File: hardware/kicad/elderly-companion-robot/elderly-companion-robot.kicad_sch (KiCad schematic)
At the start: 0 parts

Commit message: Phase 3: Create 6 hierarchical sheets
- Power_Supply (buck converter, LDO, charger)
- MCU_Core (ESP32-S3-WROOM-1, boot/EN, decoupling)
- Motor_Driver (L298N, flyback diodes, motor connectors)
- Sensors (HC-SR04 x4, MPU6050, SSD1306, I2C pull-ups)
- Audio (INMP441 mic, MAX98357A amp, speaker)
- Camera_Dock (ESP32-CAM, servos, IR beacon, dock contact)

Sheet size set to A2 for all components.

Co-Authored-By: Claude Opus 4.7 <noreply@anthropic.com>
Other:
- added sheet Audio (audio.kicad_sch)
- added sheet Camera_Dock (camera_dock.kicad_sch)
- added sheet MCU_Core (mcu_core.kicad_sch)
- added sheet Motor_Driver (motor_driver.kicad_sch)
- added sheet Power_Supply (power_supply.kicad_sch)
- added sheet Sensors (sensors.kicad_sch)

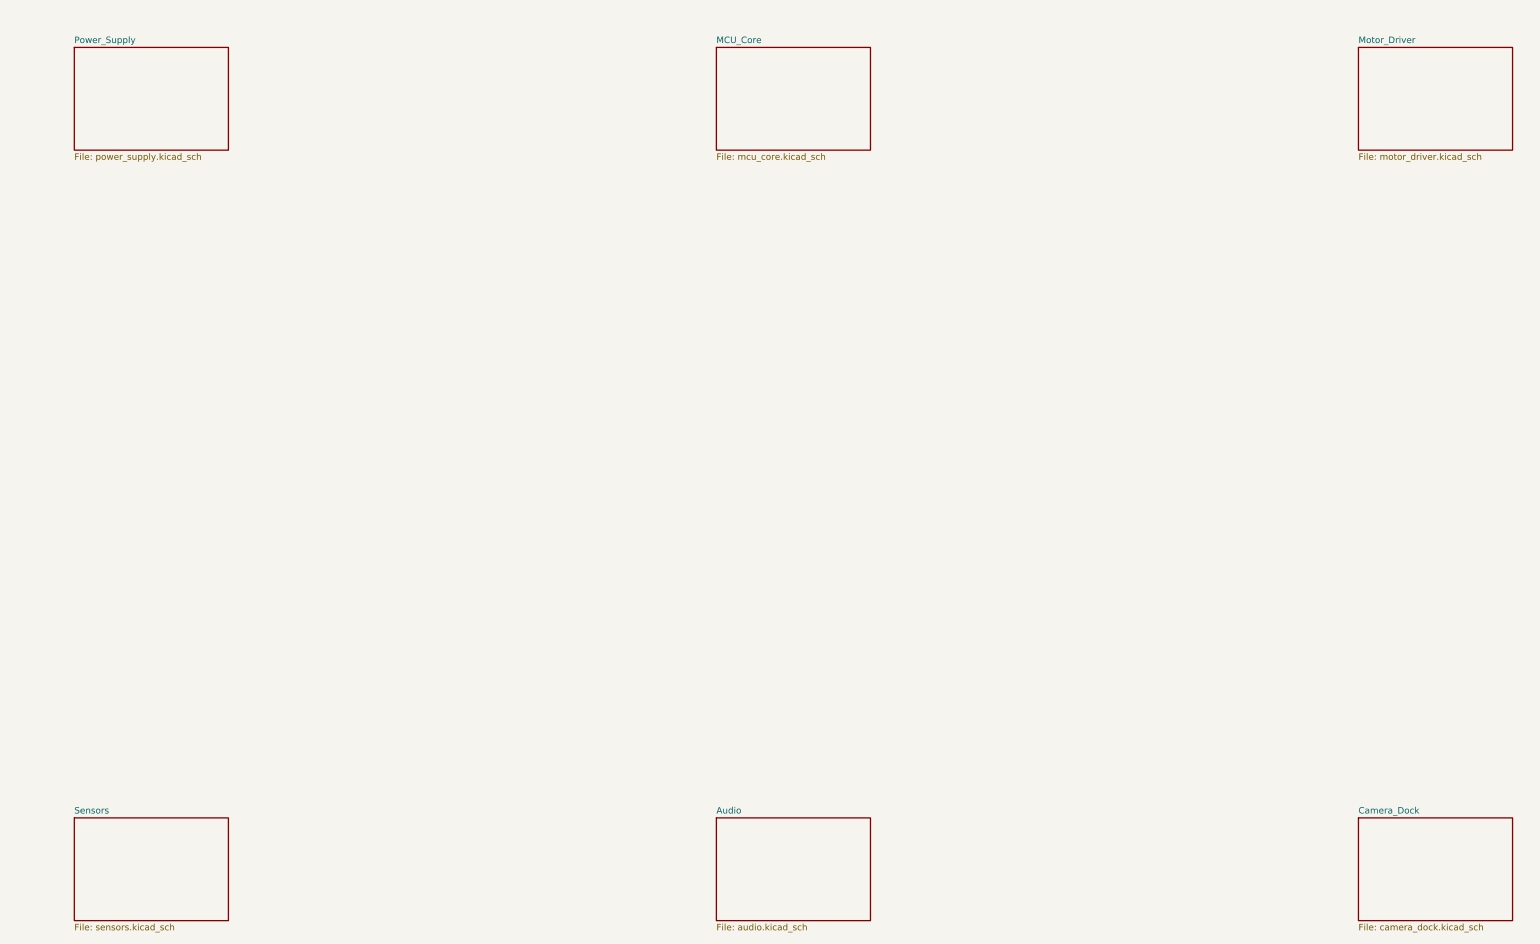
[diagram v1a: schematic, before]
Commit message: Phase 4 WIP: Power supply components placed (symbols only, not yet wired)
- LM2596S-5 buck converter (U3)
- AP2112K-3.3 LDO (U5)
- TP4056-42-ESOP8 charger (U6)
- Battery connector (J_BAT) and dock charge connector (J_DOCK)
- Passive components: C1-C5, L1, D1, R1-R3, LED1-LED2
- Power symbols: +5V, +3V3, GND, VBAT global label
- 46 ERC errors expected (pins not yet wired)

Co-Authored-By: Claude Opus 4.7 <noreply@anthropic.com>
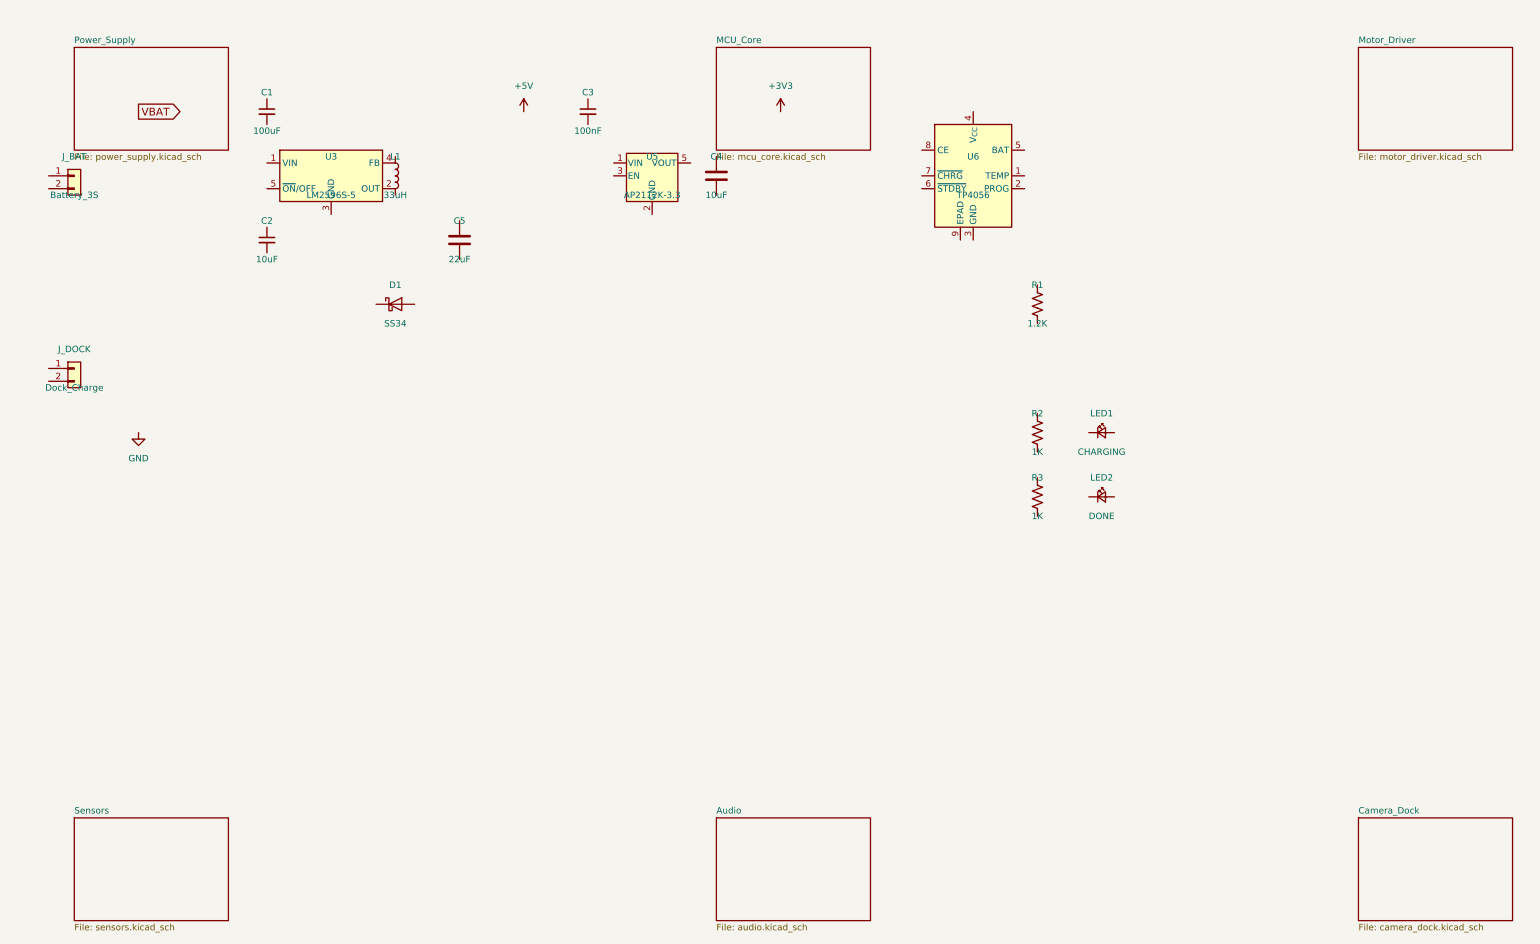
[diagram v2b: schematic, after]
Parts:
- added C1: 100uF, symbol Device:C_Small
- added C2: 10uF, symbol Device:C_Small
- added C3: 100nF, symbol Device:C_Small
- added C4: 10uF, symbol Device:C
- added C5: 22uF, symbol Device:C
- added D1: SS34, symbol Device:D_Schottky
- added J_BAT: Battery_3S, symbol Connector_Generic:Conn_01x02
- added J_DOCK: Dock_Charge, symbol Connector_Generic:Conn_01x02
- added L1: 33uH, symbol Device:L
- added LED1: CHARGING, symbol Device:LED_Small
- added LED2: DONE, symbol Device:LED_Small
- added R1: 1.2K, symbol Device:R_US
- added R2, R3: 1K, symbol Device:R_US
- added U3: LM2596S-5, symbol Regulator_Switching:LM2596S-5
- added U5: AP2112K-3.3, symbol Regulator_Linear:AP2112K-3.3
- added U6: TP4056, symbol Battery_Management:TP4056-42-ESOP8

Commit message: Phase 4 WIP: Power supply components + SIM800L LDO placed, global labels added
- Added AMS1117 adjustable LDO (U7) for SIM800L 4V rail (5V→4V)
- Added C6 100uF (SIM800L LDO input bypass)
- Added C7 10uF (SIM800L LDO output filter)
- Added C8 470uF (SIM800L burst capacitor for 2A peak)
- Added R4 1K + R5 2.2K voltage divider (sets LDO output to 4.0V)
- Added +4V global label and power symbol
- Added VBAT, +5V, +3V3 global labels
- All 27 power supply components now placed on sheet
- Detailed wiring to be completed next

Co-Authored-By: Claude Opus 4.7 <noreply@anthropic.com>
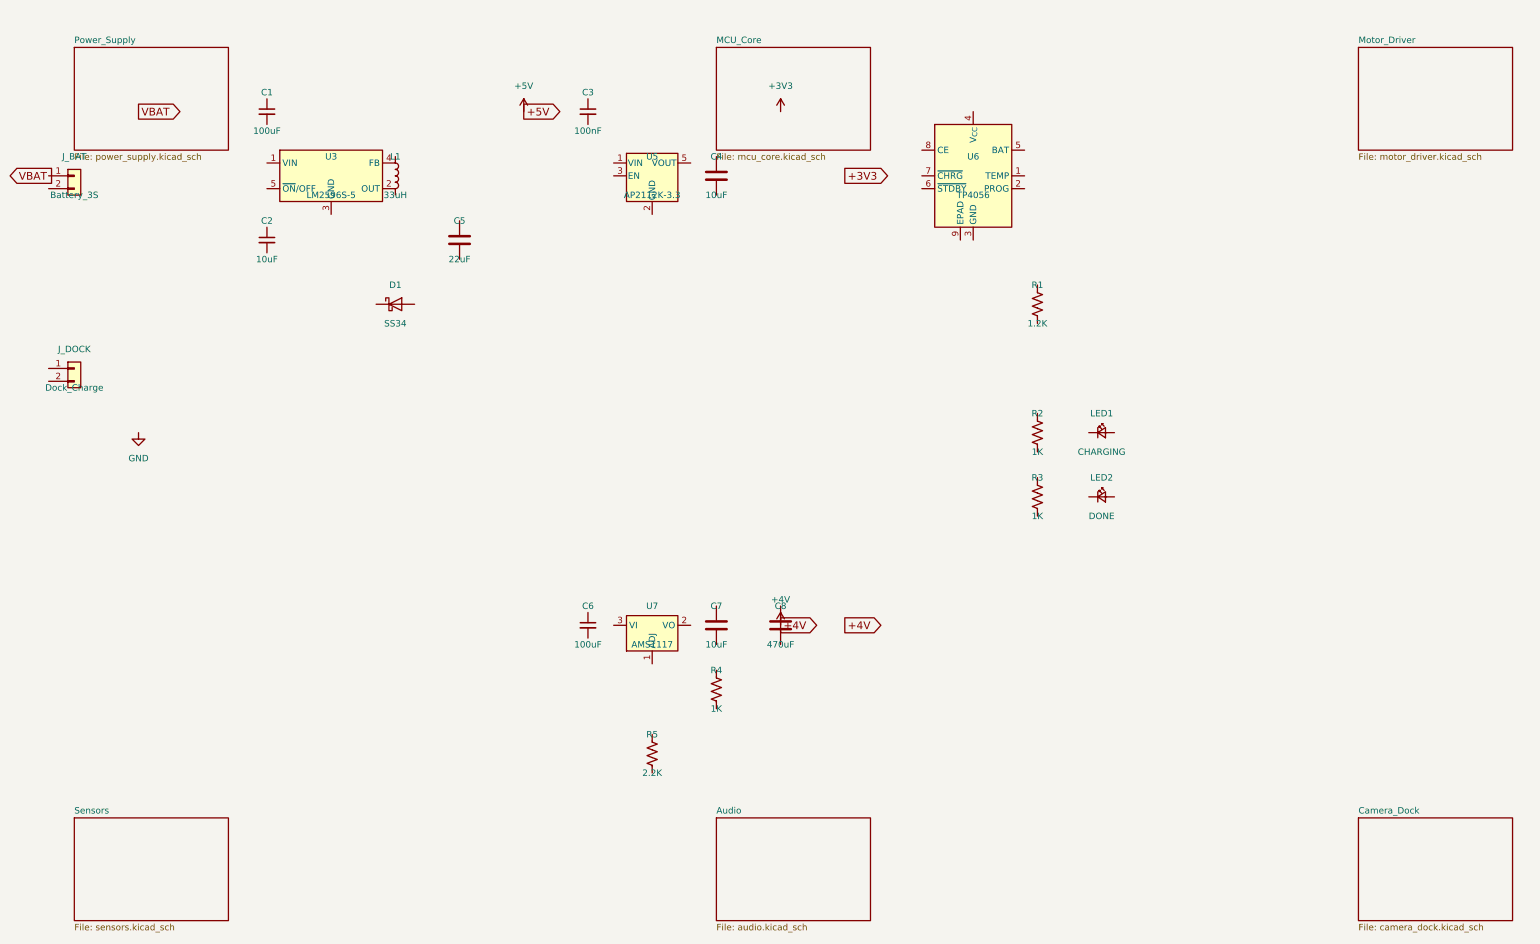
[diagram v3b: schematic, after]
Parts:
- added C6: 100uF, symbol Device:C_Small
- added C7: 10uF, symbol Device:C
- added C8: 470uF, symbol Device:C
- added R4: 1K, symbol Device:R_US
- added R5: 2.2K, symbol Device:R_US
- added U7: AMS1117, symbol Regulator_Linear:AMS1117

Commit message: Phase 4 WIP: Power supply wiring progress — key connections routed
- LM2596S-5: VIN←J_BAT, OUT→L1, L1→C5+D1, ON/OFF→GND
- AP2112K-3.3: VIN→C3, VOUT→C4, EN→VIN
- AMS1117 (SIM800L LDO): VIN←C6, VOUT→C7+C8, ADJ→R4+R5 divider
- TP4056: VCC←J_DOCK, BAT→J_BAT, PROG→R1, CHRG→R2→LED1, STDBY→R3→LED2
- Remaining wires to complete: GND connections, bypass cap ties, label assignments
- All power symbols (+5V, +3V3, +4V, GND) and global labels (VBAT, CHRG, STDBY) placed

Co-Authored-By: Claude Opus 4.7 <noreply@anthropic.com>
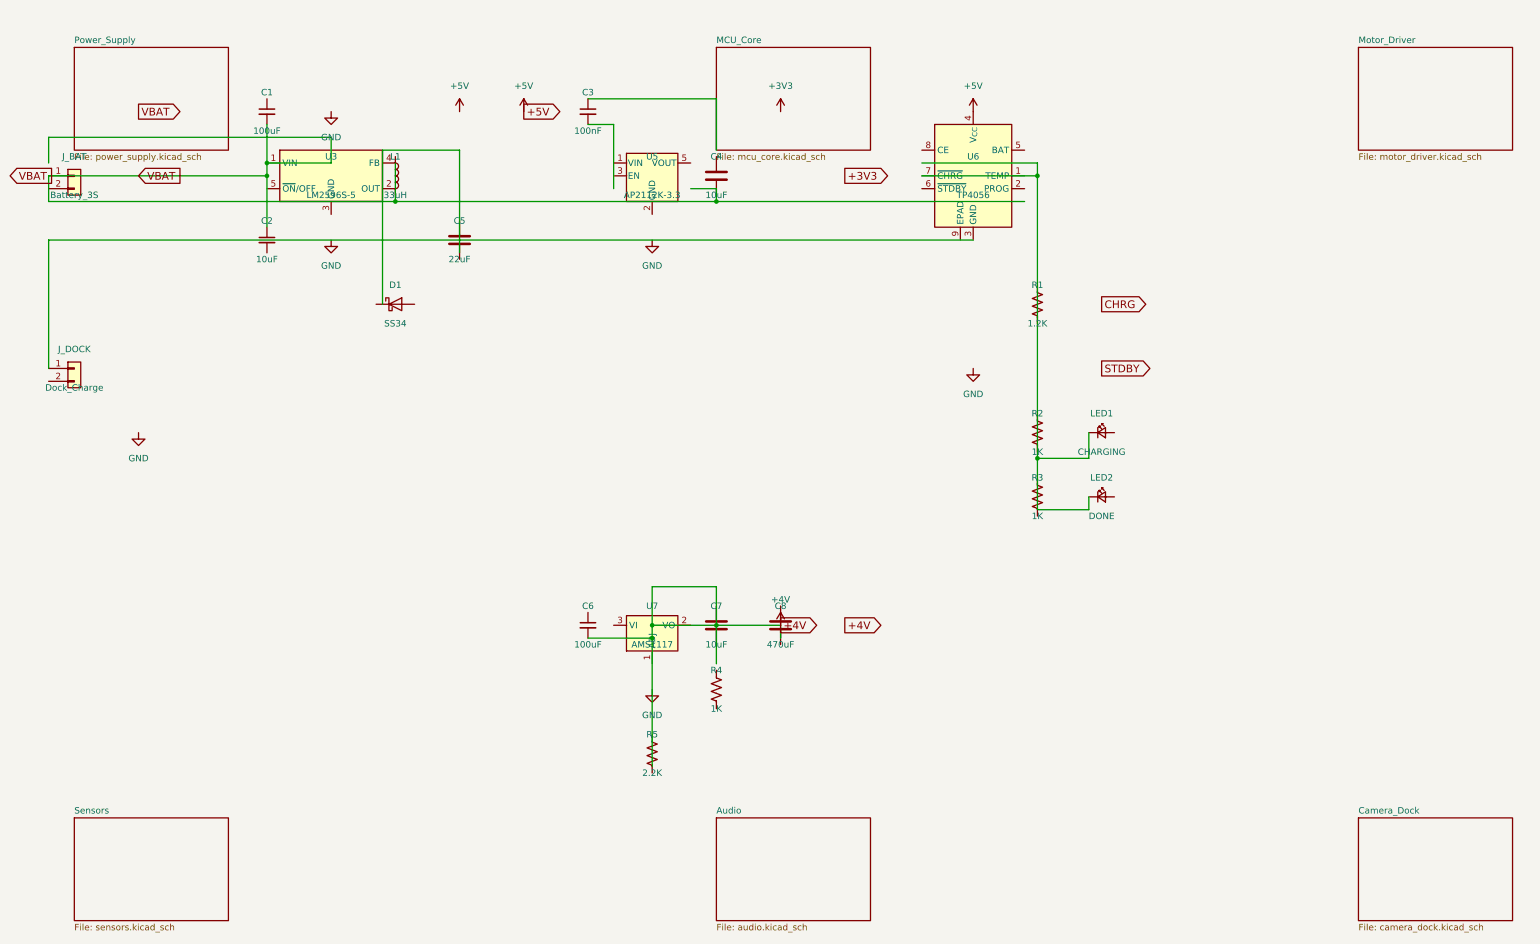
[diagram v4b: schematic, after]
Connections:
- net +4V: now also C6.2
- net +5V: now also U6.4 (V_{CC})
- net VBAT: now also C1.2, C2.1, J_BAT.1 (Pin_1)
- net at U6.3 (GND): now also J_DOCK.1 (Pin_1)
- net at U6.7 (~{CHRG}): now also LED1.1 (K), LED2.1 (K)

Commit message: Phase 5 WIP: MCU Core sheet — ESP32-S3-WROOM-1, boot circuit, decoupling caps
- ESP32-S3-WROOM-1-N16R8 (U1) placed at center of sheet
- R10 10K (EN pull-up), R11 10K (GPIO12 pull-down), SW1 (BOOT button)
- C10, C11 100nF + C12 10uF decoupling caps
- +3V3 and GND power symbols
- 27 hierarchical labels for cross-sheet signals: I2C (SDA/SCL), I2S (BCLK/LRCLK/DOUT/DIN),
  Motor (ENA/IN1-4/ENB), Servo (PAN/TILT), IR (TX/RX), Ultrasonic (4x TRIG/ECHO),
  SIM800L (TX/RX/PWRKEY)
- GPIO-to-label wiring to be completed in KiCad editor

Co-Authored-By: Claude Opus 4.7 <noreply@anthropic.com>
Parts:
- removed C1, C6: 100uF, symbol Device:C_Small
- removed C2: 10uF, symbol Device:C_Small
- removed C3: 100nF, symbol Device:C_Small
- removed C4, C7: 10uF, symbol Device:C
- removed C5: 22uF, symbol Device:C
- removed C8: 470uF, symbol Device:C
- removed D1: SS34, symbol Device:D_Schottky
- removed J_BAT: Battery_3S, symbol Connector_Generic:Conn_01x02
- removed J_DOCK: Dock_Charge, symbol Connector_Generic:Conn_01x02
- removed L1: 33uH, symbol Device:L
- removed LED1: CHARGING, symbol Device:LED_Small
- removed LED2: DONE, symbol Device:LED_Small
- removed R1: 1.2K, symbol Device:R_US
- removed R2, R3, R4: 1K, symbol Device:R_US
- removed R5: 2.2K, symbol Device:R_US
- removed U3: LM2596S-5, symbol Regulator_Switching:LM2596S-5
- removed U5: AP2112K-3.3, symbol Regulator_Linear:AP2112K-3.3
- removed U6: TP4056, symbol Battery_Management:TP4056-42-ESOP8
- removed U7: AMS1117, symbol Regulator_Linear:AMS1117
- added C10, C11: 100nF, symbol Device:C
- added C12: 10uF, symbol Device:C_Small
- added R10, R11: 10K, symbol Device:R_US
- added SW1: BOOT, symbol Device:SW_Push
- added U1: ESP32-S3-WROOM-1-N16R8, symbol RF_Module:ESP32-S3-WROOM-1
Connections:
- new net: U1.1 (GND), U1.40 (GND), U1.41 (GND)
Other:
- removed sheet Audio
- removed sheet Camera_Dock
- removed sheet MCU_Core
- removed sheet Motor_Driver
- removed sheet Power_Supply
- removed sheet Sensors

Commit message: Phase 6 WIP: Motor Driver sheet — L298N, flyback diodes, motor connectors
- L298N (U8) dual H-bridge motor driver placed
- 2x motor connectors (J_MOTOR_L, J_MOTOR_R)
- 8x 1N4007 flyback diodes (D2-D9)
- Hierarchical labels: MOTOR_ENA, MOTOR_IN1-4, MOTOR_ENB
- Power symbols: +5V, VBAT, GND
- Wiring to be completed in KiCad editor

Co-Authored-By: Claude Opus 4.7 <noreply@anthropic.com>
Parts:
- removed C10, C11: 100nF, symbol Device:C
- removed C12: 10uF, symbol Device:C_Small
- removed R10, R11: 10K, symbol Device:R_US
- removed SW1: BOOT, symbol Device:SW_Push
- removed U1: ESP32-S3-WROOM-1-N16R8, symbol RF_Module:ESP32-S3-WROOM-1
- added D2, D3, D4, D5, D6, D7, D8, D9: 1N4007, symbol Device:D
- added J_MOTOR_L: Motor_Left, symbol Connector_Generic:Conn_01x02
- added J_MOTOR_R: Motor_Right, symbol Connector_Generic:Conn_01x02
- added U8: L298N, symbol Driver_Motor:L298N

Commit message: Phase 7 WIP: Sensors sheet — HC-SR04, MPU6050, SSD1306, I2C pull-ups
- 4x HC-SR04 ultrasonic connectors (J_US_F/B/L/R) with voltage divider resistors
- 8x resistors (R20-R27) for Echo voltage dividers (1K+2K each, 5V→3.33V)
- MPU6050_GY521 IMU (U_IMU) on I2C
- SSD1306 OLED (U_OLED) on I2C
- 2x 4.7K I2C pull-ups (R30, R31) on SDA/SCL
- Hierarchical labels: I2C_SDA/SCL, US_FRONT/BACK/LEFT/RIGHT_TRIG/ECHO
- Power: +5V (HC-SR04), +3V3 (MPU6050, OLED), GND

Co-Authored-By: Claude Opus 4.7 <noreply@anthropic.com>
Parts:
- removed D2, D3, D4, D5, D6, D7, D8, D9: 1N4007, symbol Device:D
- removed J_MOTOR_L: Motor_Left, symbol Connector_Generic:Conn_01x02
- removed J_MOTOR_R: Motor_Right, symbol Connector_Generic:Conn_01x02
- removed U8: L298N, symbol Driver_Motor:L298N
- added J_US_B: HC-SR04_Back, symbol Connector_Generic:Conn_01x04
- added J_US_F: HC-SR04_Front, symbol Connector_Generic:Conn_01x04
- added J_US_L: HC-SR04_Left, symbol Connector_Generic:Conn_01x04
- added J_US_R: HC-SR04_Right, symbol Connector_Generic:Conn_01x04
- added R20, R22, R24, R26: 1K, symbol Device:R_US
- added R21, R23, R25, R27: 2K, symbol Device:R_US
- added R30, R31: 4.7K, symbol Device:R_US
- added U_IMU: MPU6050, symbol Device:MPU6050_GY521
- added U_OLED: SSD1306, symbol Device:SSD1306_OLED_128x64

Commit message: Phase 8 WIP: Audio sheet — INMP441 mic, MAX98357A amp, speaker connector
- INMP441 I2S MEMS mic connector (J_MIC, 6-pin)
- MAX98357A I2S amplifier connector (J_SPK, 3-pin)
- Bypass caps: C20 100nF (mic VDD), C21 100nF + C22 10uF (amp VDD)
- R40 10K pull-down on GPIO12/LRCLK (strapping pin)
- Hierarchical labels: I2S_BCLK, I2S_LRCLK, I2S_DOUT, I2S_DIN
- Power: +3V3 (mic), +5V (amp), GND

Co-Authored-By: Claude Opus 4.7 <noreply@anthropic.com>
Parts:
- removed J_US_B: HC-SR04_Back, symbol Connector_Generic:Conn_01x04
- removed J_US_F: HC-SR04_Front, symbol Connector_Generic:Conn_01x04
- removed J_US_L: HC-SR04_Left, symbol Connector_Generic:Conn_01x04
- removed J_US_R: HC-SR04_Right, symbol Connector_Generic:Conn_01x04
- removed R20, R22, R24, R26: 1K, symbol Device:R_US
- removed R21, R23, R25, R27: 2K, symbol Device:R_US
- removed R30, R31: 4.7K, symbol Device:R_US
- removed U_IMU: MPU6050, symbol Device:MPU6050_GY521
- removed U_OLED: SSD1306, symbol Device:SSD1306_OLED_128x64
- added C20: 100nF, symbol Device:C_Small
- added C21: 100nF, symbol Device:C
- added C22: 10uF, symbol Device:C
- added J_MIC: INMP441_Mic, symbol Connector_Generic:Conn_01x06
- added J_SPK: MAX98357A_Amp, symbol Connector_Generic:Conn_01x03
- added R40: 10K, symbol Device:R_US
